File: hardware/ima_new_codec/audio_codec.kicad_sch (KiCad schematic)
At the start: 19 parts, among them IC1 TLV320AIC3204IRHBR, J2 AudioJack2, J3 AudioJack2, J4 AudioJack2, J5 AudioJack2

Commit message: changes to input/output stages
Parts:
- removed C10, C11, C3, C4, C7, C8: 0.1u, symbol Device:C
- removed C6, C9: 4700p, symbol Device:C
- removed J2, J3, J4, J5: AudioJack2, symbol Connector_Audio:AudioJack2
- removed R1, R2, R3, R4: 1k, symbol Device:R
- added C13: 10u, symbol Device:C
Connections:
- net GND: now also C13.1
- net INL: now reaches IC1.14 (IN1_R)
- net INL: now also IC1.13 (IN1_L)
- net OUTL: now reaches IC1.23 (LOR)
- net OUTR: now reaches IC1.22 (LOL)
- net CODECREF: now reaches IC1.18 (REF)
- net CODECREF: now also C13.2
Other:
- added sheet Input Output Channels (in_outs.kicad_sch)
- moved on the sheet: C12, C5, IC1

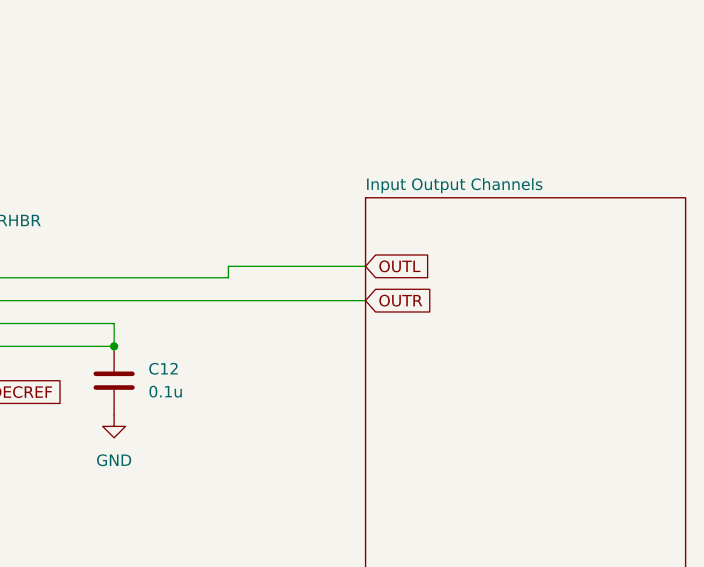
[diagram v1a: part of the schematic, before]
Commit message: changes to in/out stages
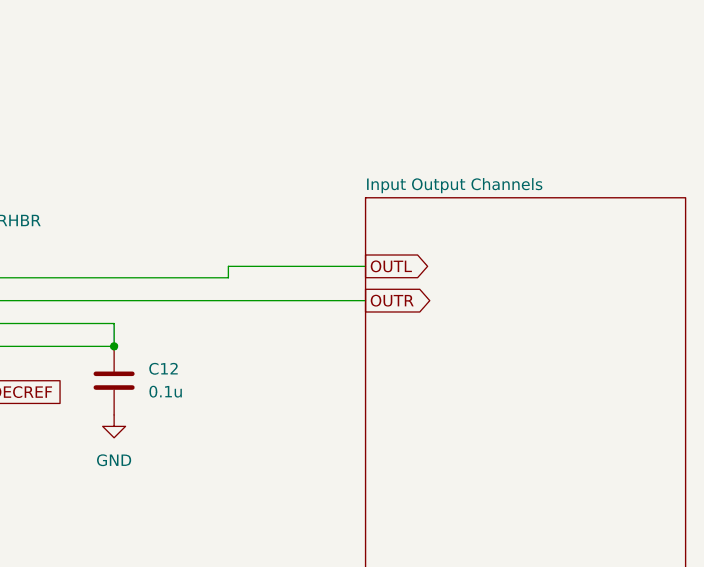
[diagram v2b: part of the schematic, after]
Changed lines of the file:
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@@
 	)
 	(global_label "OUTR"
-		(shape input)
+		(shape output)
 		(at 208.28 85.09 0)
 		(fields_autoplaced yes)
@@
 	)
 	(global_label "OUTL"
-		(shape input)
+		(shape output)
 		(at 208.28 81.28 0)
 		(fields_autoplaced yes)
